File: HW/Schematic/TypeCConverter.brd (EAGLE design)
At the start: 29.1 x 35.4 mm, 44 parts, among them U2 CP2104

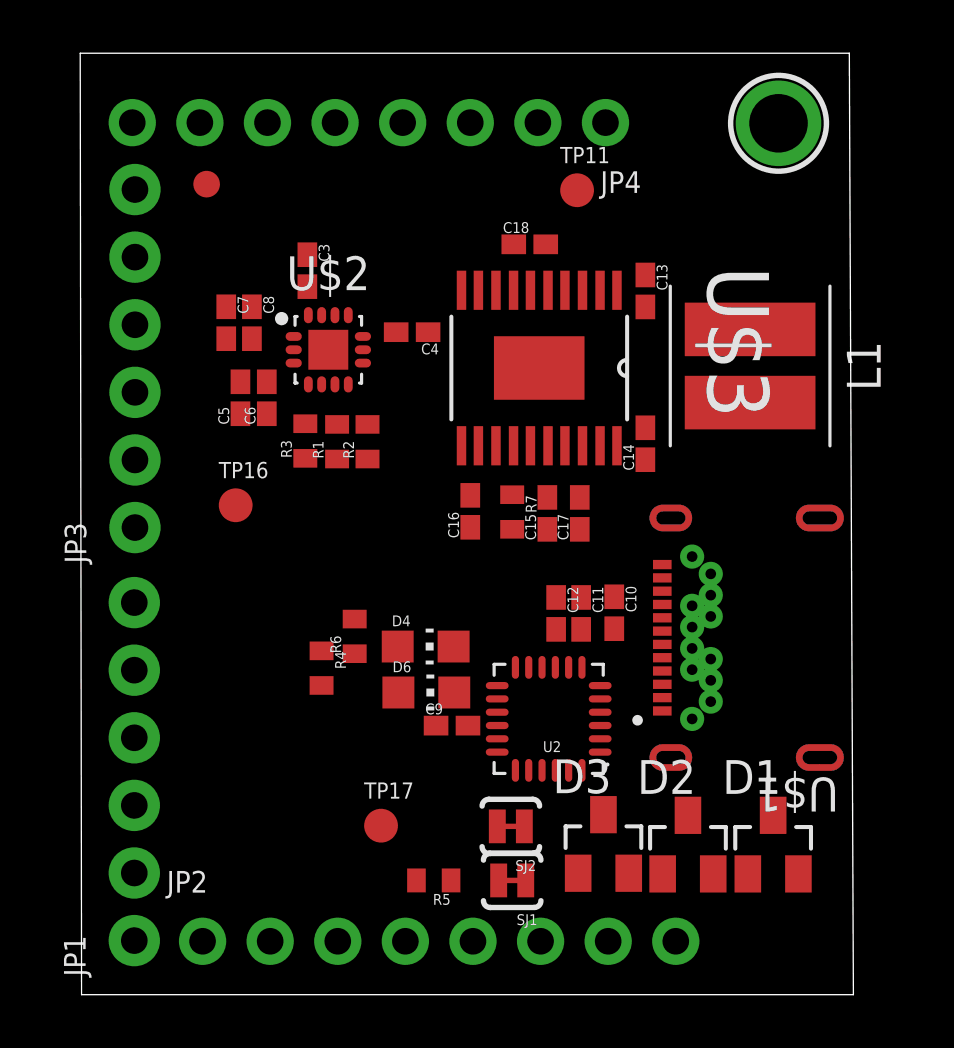
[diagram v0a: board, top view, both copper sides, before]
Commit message: Finish pre layout
Generate layout pdfs
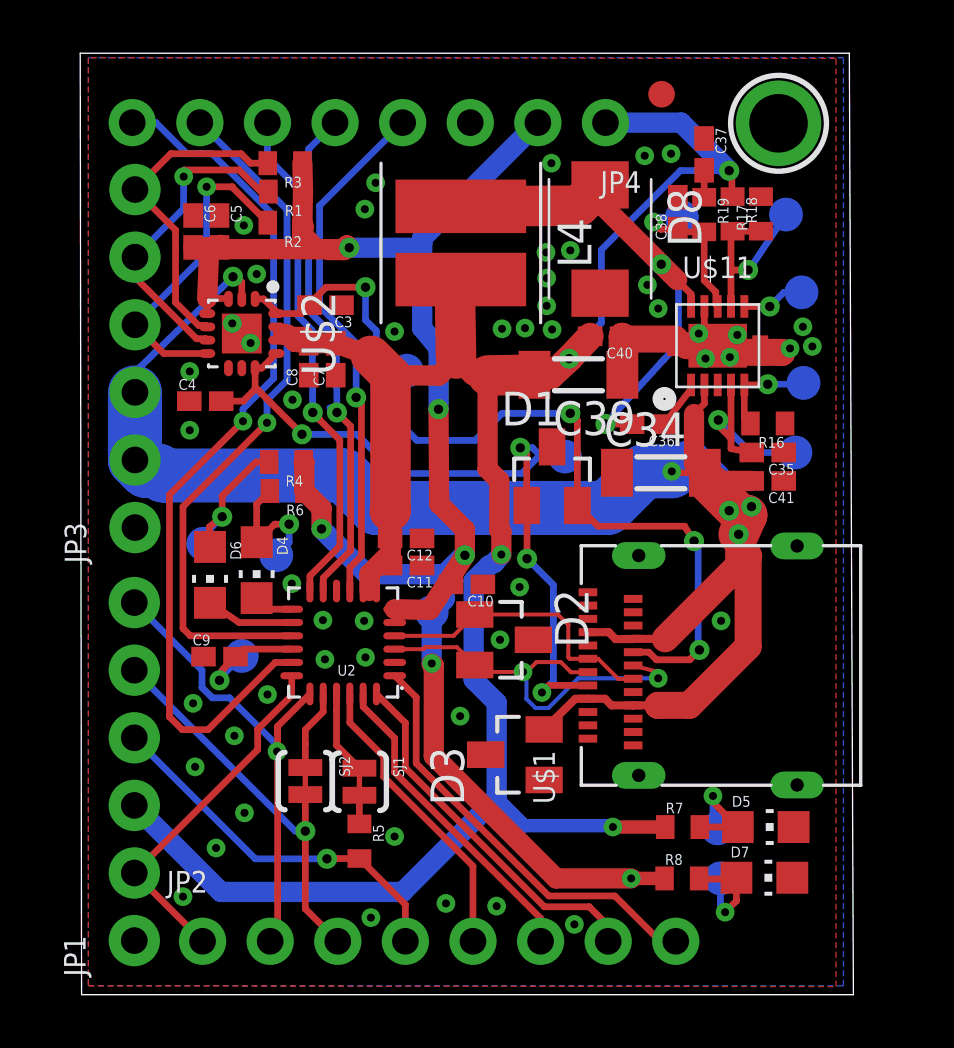
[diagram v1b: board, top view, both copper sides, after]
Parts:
- removed C13, C14, C15: 100nF, capacitor:C0402K
- removed C16: 4.7uF, capacitor:C0402K
- removed C17: 22uF, capacitor:C0402K
- removed C18: 10uF, capacitor:C0402K
- removed L1: 4.7uH, Inductor:DFN600X600X420-2
- removed U$3: TPS55165QPWPRQ1, TPS55165QPWPRQ1:SOP65P640X120-21N
- added C34: 2.2uF, capacitor:SM-1206
- added C35: 0.01uF, capacitor:C0402K
- added C36, C41: 0.1uF, capacitor:C0402K
- added C37: 2.7nF, capacitor:C0402K
- added C38: 6.8pF, capacitor:C0402K
- added C39: 47uF, capacitor:SM-1206
- added C40: 100nF, capacitor:C0402K
- added D5, D7: LED, LED:CHIP-LED0805
- added D8: DIODESMB, Diode:SMBJ
- added L4: 10uH, Inductor:DFN600X600X420-2
- added R16: 90.9k, resistor:R0402
- added R17, R18: (no value), resistor:R0402
- added R19: 76.8k, resistor:R0402
- added R8: 4k7, resistor:R0402
- added TP1, TP10, TP12, TP3, TP4, TP5, TP6, TP7, TP8, TP9: CP_RESET, testpad:B1,27
- added U$11: TPS57140QDRCRQ1, PMIC:VSON10
- R7: value 100k -> 4k7
- U$1: value USB-TYPE-CTYPECHYBRIDOK -> USB-TYPE-CTYPEC_SMT; device lio:USBTYPECHYBRIDOK -> lio:TYPECSMT
- moved TP2 17.4 mm to (21.8, 33.8)
- moved D1 16.1 mm to (17.7, 19.5)
- moved R7 13.5 mm to (22.6, 6.30), turned to 0 degrees
- moved R3 10.5 mm to (7.65, 31.2), turned to 180 degrees
- moved D2 10.3 mm to (15.9, 13.3), turned to 270 degrees
- moved R1 9.59 mm to (7.67, 30.2), turned to 180 degrees
- moved TP11 9.26 mm to (27.1, 26.4), flipped to the bottom
- moved D6 9.25 mm to (4.83, 15.8), turned to 180 degrees
- moved C9 9.11 mm to (5.18, 12.7)
- moved R2 8.79 mm to (7.65, 29.0), turned to 180 degrees
- moved TP16 8.39 mm to (13.2, 14.4), flipped to the bottom
- moved TP17 8.25 mm to (6.02, 12.7), flipped to the bottom
- moved U2 8.24 mm to (9.83, 13.2)
- moved C4 8.19 mm to (4.65, 22.3), turned to 0 degrees
- moved SJ2 7.91 mm to (8.41, 8.03), turned to 270 degrees
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- renumbered U$19 to GND
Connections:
- removed net BST1: C13.1, U$3.3
- removed net BST2: C14.1, U$3.19
- removed net L2: C14.2, L1.2, U$3.20
- removed net PG: R7.2, U$3.15
- removed net VREG: C16.2, U$3.11, U$3.12
- new net 3V45LEDWP: D7.A, R8.2, TP12.TP
- new net 5VLEDWP: D5.A, R7.2, TP10.TP
- new net BOOT: C36.1, U$11.1
- new net CLK: R16.2, TP3.TP, U$11.5
- new net COMP: C38.1, R19.2, TP9.TP, U$11.8
- new net COMP_S: C37.2, R19.1
- new net EN: U$11.3
- new net PGOOD: TP11.TP, U$11.6
- new net SS/TR: C35.2, TP1.TP, U$11.4
- new net VSNS: R17.1, R18.2, TP4.TP, U$11.7
- net 5V: now also C39.2, C40.2, JP1.3, JP4.1, L4.2, R18.1; no longer C15.2, C17.2, U$3.16, U$3.17
- net CC1: now also TP7.TP
- net CC2: now also TP8.TP
- net CP_RESET: no longer TP11.TP
- net CP_VDD_3V45: now also R8.1
- net GND: now also C34.1, C35.1, C37.1, C38.2, C39.1, C40.1, C41.1, D5.C, D7.C, D8.A, R16.1, R17.2, U$11.11, U$11.12, U$11.13, U$11.14, U$11.15, U$11.9; no longer C15.1, C16.1, C17.1, C18.1, U$3.1, U$3.10, U$3.13, U$3.14, U$3.18, U$3.21
- net L1: now also C36.2, D8.C, L4.1, U$11.10; no longer C13.2, L1.1, U$3.2
- net RXLEDWP: now also TP6.TP
- net TXLEDWP: now also TP5.TP
- net VBUS: now also C34.2, C41.2, U$11.2; no longer C18.2, JP1.3, JP4.1, U$3.4, U$3.5, U$3.6
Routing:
- net 5V: track 0.00 -> 90.5 mm, vias 0 -> 4
- net CP_VDD_3V45: track 0.00 -> 70.0 mm, vias 0 -> 6
- net VBUS: track 0.00 -> 68.0 mm, vias 0 -> 5
- net CC2: track 0.00 -> 34.7 mm, vias 0 -> 4
- net SUSPEND: track 0.00 -> 33.1 mm, vias 0 -> 1
- net CC1: track 0.00 -> 29.1 mm, vias 0 -> 4
- net /SUSPEND: track 0.00 -> 26.2 mm, vias 0 -> 1
- net L1: track 0.00 -> 19.9 mm, vias 0 -> 2
- net CP_RESET: track 0.00 -> 19.7 mm, vias 0 -> 1
- net GPIO3: track 0.00 -> 19.4 mm, vias 0 -> 1
- net GPIO2: track 0.00 -> 19.2 mm, vias 0 -> 1
- net RTS: track 0.00 -> 18.1 mm, vias 0 -> 1
- net USB_P: track 0.00 -> 16.4 mm, vias 0 -> 2
- net RI: track 0.00 -> 16.1 mm
- net RXD: track 0.00 -> 14.9 mm, vias 0 -> 1
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- added copper zone on layer 1, net GND
- added copper zone on layer 16, net GND

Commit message: Add BOM
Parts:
- removed C9: 10uF, capacitor:C0402K
- removed TP17: VPP, testpad:B1,27
- R17: value (none) -> 10k 1%
- R18: value (none) -> 52.5k 1%
- moved TP9 0.38 mm to (22.9, 29.2)
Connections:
- removed net VPP: C9.2, TP17.TP, U2.16
- net GND: no longer C9.1
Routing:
- net VPP: track 4.59 -> 0.00 mm, vias 1 -> 0
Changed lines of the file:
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@@
 <grid distance="1" unitdist="mil" unit="mil" style="lines" multiple="1" display="yes" altdistance="0.000123031496" altunitdist="mil" altunit="mil"/>
 <layers>
-<layer number="1" name="Top" color="4" fill="1" visible="no" active="yes"/>
+<layer number="1" name="Top" color="4" fill="1" visible="yes" active="yes"/>
 <layer number="2" name="Route2" color="1" fill="3" visible="no" active="no"/>
 <layer number="3" name="Route3" color="4" fill="3" visible="no" active="no"/>
@@
 <element name="C7" library="capacitor" package="C0402K" package3d_urn="urn:adsk.eagle:package:23679/2" value="10uF" x="9.5504" y="23.876" rot="R90"/>
 <element name="C8" library="capacitor" package="C0402K" package3d_urn="urn:adsk.eagle:package:23679/2" value="100nF" x="8.5344" y="23.876" rot="R90"/>
-<element name="C9" library="capacitor" package="C0402K" package3d_urn="urn:adsk.eagle:package:23679/2" value="10uF" x="5.1816" y="12.7"/>
 <element name="D1" library="diode" library_urn="urn:adsk.eagle:library:210" package="SOT23" package3d_urn="urn:adsk.eagle:package:43389/2" value="PESD1CAN" x="17.6784" y="19.4818"/>
 <element name="D2" library="diode" library_urn="urn:adsk.eagle:library:210" package="SOT23" package3d_urn="urn:adsk.eagle:package:43389/2" value="PESD1CAN" x="15.875" y="13.335" rot="R270"/>
@@
 <attribute name="TP_SIGNAL_NAME" value="" x="13.1572" y="14.3764" size="1.778" layer="28" rot="MR0" display="off"/>
 </element>
-<element name="TP17" library="testpad" package="B1,27" value="VPP" x="6.0198" y="12.7254" rot="MR0">
-<attribute name="TP_SIGNAL_NAME" value="" x="6.0198" y="12.7254" size="1.778" layer="28" rot="MR0" display="off"/>
-</element>
 <element name="TP2" library="adafruit" package="FIDUCIAL_1MM" value="FIDUCIAL" x="21.7932" y="33.8328"/>
 <element name="U$1" library="lio" package="TYPECSMT" value="USB-TYPE-CTYPEC_SMT" x="24.765" y="12.3698" rot="R90"/>
@@
 <element name="C36" library="capacitor" package="C0402K" package3d_urn="urn:adsk.eagle:package:23679/2" value="0.1uF" x="21.2852" y="21.4376" rot="R180"/>
 <element name="L4" library="Inductor" package="DFN600X600X420-2" package3d_urn="urn:adsk.eagle:package:6883134/1" value="10uH" x="14.2494" y="28.2448" rot="R270"/>
-<element name="R17" library="resistor" package="R0402" package3d_urn="urn:adsk.eagle:package:970935/2" value="" x="25.527" y="29.337" rot="R90"/>
-<element name="R18" library="resistor" package="R0402" package3d_urn="urn:adsk.eagle:package:970935/2" value="" x="24.4602" y="29.337" rot="R270"/>
+<element name="R17" library="resistor" package="R0402" package3d_urn="urn:adsk.eagle:package:970935/2" value="10k 1%" x="25.527" y="29.337" rot="R90"/>
+<element name="R18" library="resistor" package="R0402" package3d_urn="urn:adsk.eagle:package:970935/2" value="52.5k 1%" x="24.4602" y="29.337" rot="R270"/>
 <element name="C37" library="capacitor" package="C0402K" package3d_urn="urn:adsk.eagle:package:23679/2" value="2.7nF" x="23.3934" y="31.5722" rot="R270"/>
 <element name="C38" library="capacitor" package="C0402K" package3d_urn="urn:adsk.eagle:package:23679/2" value="6.8pF" x="22.4028" y="29.3624" rot="R90"/>
@@
 <attribute name="TP_SIGNAL_NAME" value="" x="12.2174" y="23.4442" size="1.778" layer="28" rot="MR270" display="off"/>
 </element>
-<element name="TP9" library="testpad" package="B1,27" value="CP_RESET" x="22.5552" y="29.21" rot="MR0">
-<attribute name="TP_SIGNAL_NAME" value="" x="22.5552" y="29.21" size="1.778" layer="28" rot="MR0" display="off"/>
+<element name="TP9" library="testpad" package="B1,27" value="CP_RESET" x="22.9362" y="29.21" rot="MR0">
+<attribute name="TP_SIGNAL_NAME" value="" x="22.9362" y="29.21" size="1.778" layer="28" rot="MR0" display="off"/>
 </element>
 <element name="R7" library="resistor" package="R0402" package3d_urn="urn:adsk.eagle:package:970935/2" value="4k7" x="22.5806" y="6.2992"/>
@@
 <contactref element="C12" pad="1"/>
 <contactref element="U2" pad="2"/>
-<contactref element="C9" pad="1"/>
 <contactref element="JP3" pad="1"/>
 <contactref element="U$1" pad="A1"/>
@@
 <via x="22.1488" y="31.5976" extent="1-16" drill="0.3"/>
 <via x="18.5166" y="2.6416" extent="1-16" drill="0.3"/>
-<via x="24.0284" y="14.0462" extent="1-16" drill="0.3"/>
+<via x="24.0284" y="13.97" extent="1-16" drill="0.3"/>
 </signal>
 <signal name="VBUS">
@@
 <wire x1="23.4178" y1="19.6088" x2="22.48358125" y2="19.6088" width="0.254" layer="1"/>
 <wire x1="22.48358125" y1="19.6088" x2="22.176490625" y2="19.661890625" width="0.254" layer="1"/>
-</signal>
-<signal name="VPP">
-<contactref element="U2" pad="16"/>
-<contactref element="C9" pad="2"/>
-<contactref element="TP17" pad="TP"/>
-<via x="5.1816" y="11.811" extent="1-16" drill="0.35"/>
-<wire x1="5.7816" y1="12.7" x2="5.3235" y2="12.2419" width="0.254" layer="1"/>
-<wire x1="5.3235" y1="12.2419" x2="5.3235" y2="12.21426875" width="0.254" layer="1"/>
-<wire x1="5.3235" y1="12.21426875" x2="5.2578" y2="12.14856875" width="0.254" layer="1"/>
-<wire x1="5.2578" y1="12.14856875" x2="5.1816" y2="11.811" width="0.254" layer="1"/>
-<wire x1="5.1816" y1="11.811" x2="5.2578" y2="11.9634" width="0.254" layer="16"/>
-<wire x1="5.2578" y1="11.9634" x2="6.0198" y2="12.7254" width="0.254" layer="16"/>
-<wire x1="7.8952" y1="12.9834" x2="6.065" y2="12.9834" width="0.254" layer="1"/>
-<wire x1="6.065" y1="12.9834" x2="5.7816" y2="12.7" width="0.254" layer="1"/>
 </signal>
 <signal name="CP_RESET">
@@
 <via x="21.4884" y="29.0322" extent="1-16" drill="0.3"/>
 <wire x1="21.4884" y1="29.0322" x2="21.6662" y2="29.21" width="0.254" layer="16"/>
-<wire x1="21.6662" y1="29.21" x2="22.5552" y2="29.21" width="0.254" layer="16"/>
+<wire x1="21.6662" y1="29.21" x2="22.9362" y2="29.21" width="0.254" layer="16"/>
 </signal>
 <signal name="PGOOD">
